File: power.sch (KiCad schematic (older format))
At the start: 68 parts, among them J1 PEN_SEL, J2 PEN_SEL, J3 USB_C_Receptacle_USB2.0, U10 74LVC1G02, U11 UTC2000, U4 TLV62569ADDC, U5 TPS62A01A-SOT563, U6 TPS62A01A-SOT563, U7 TLV62569ADDC, U9 TLV62569ADDC

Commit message: WIP: point before we change to OSH/relaxed process
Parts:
- added C91, C92: 100n, Capacitor_SMD:C_0603_1608Metric, symbol fmc:100nF_603
- added C93: 220u, Capacitor_Tantalum_SMD:CP_EIA-6032-28_Kemet-C, symbol Device:CP1_Small
- added C94: 1n, Capacitor_SMD:C_0603_1608Metric, symbol fmc:100nF_603
- added Q2: SSM6N35AFE, proj_footprints:SOT-563-adjusted, symbol Device:Q_DUAL_NMOS_S1G1D2S2G2D1
- added Q3: Si3477, Package_TO_SOT_SMD:TSOT-23-6, symbol fmc:Q_PMOS_DDGSDD
- added R75, R76, R78: 100k, Resistor_SMD:R_0603_1608Metric, symbol Device:R_Small
- added R77: 47, Resistor_SMD:R_1206_3216Metric, symbol Device:R_Small
- added R79: 10k, Resistor_SMD:R_0603_1608Metric, symbol Device:R_Small
- added U13: TPS3808DBV, Package_TO_SOT_SMD:SOT-23-6, symbol fmc:TPS3808DBV
- J1: value PEN_SEL -> CUR_SEL
- U10: value 74LVC1G02 -> 74VHC1G03; symbol fmc:74LVC1G02 -> fmc:74VHC1G03
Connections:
- net labels added: POWER_CYCLE
- wire segments 224 -> 267
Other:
- note added: "When using the inrush current limiter\nthe sense threshold matters!\nResistor values depend on TPS3808\nvariant's threshold!"
- note added: "optional inrush current\nlimiter (USB)."
- moved on the sheet: J1, J2, R52, R53, R62

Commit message: further work...
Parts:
- removed D9: LED, LED_SMD:LED_0603_1608Metric, symbol Device:LED
- removed R51: 1k, Resistor_SMD:R_0603_1608Metric, symbol Device:R_Small
- removed U10: 74VHC1G03, Package_TO_SOT_SMD:SOT-23-5, symbol fmc:74VHC1G03
- added Q6: Si3477, Package_TO_SOT_SMD:TSOT-23-6, symbol fmc:Q_PMOS_DDGSDD
- added Q7: SSM6N35AFE, proj_footprints:SOT-563-adjusted, symbol Device:Q_DUAL_NMOS_S1G1D2S2G2D1
- added TP14: TestPoint, TestPoint:TestPoint_Pad_D1.0mm, symbol Connector:TestPoint
- added U10: 74LVC1G06, Package_TO_SOT_SMD:SOT-353_SC-70-5, symbol fmc:74LVC1G38
- J2: footprint Connector_PinHeader_2.54mm:PinHeader_2x03_P2.54mm_Vertical -> Connector_PinHeader_2.54mm:PinHeader_2x02_P2.54mm_Vertical; symbol Connector_Generic:Conn_02x03_Odd_Even -> Connector_Generic:Conn_02x02_Odd_Even
- R22, R23, R24, R25, R33: value 10k -> 100k
- R40: value 45.9k -> 10k
- R45: value 10.2k -> 45k3
- R52: value 100k -> 10k; Manufacturer Yageo -> (none); Part RC0603FR-07100KL -> (none)
- R75: value 100k -> 45.3k
- R76: value 100k -> 10k
- R77: value 47 -> 50; footprint Resistor_SMD:R_1206_3216Metric -> Resistor_SMD:R_0603_1608Metric
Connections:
- net +5V: now also Q6.4 (S), U10.5 (VCC); no longer R35.2, R52.2
- net GND: now also R35.2, R52.2, Q7.1 (S), Q7.4 (S), U10.3 (GND); no longer J2.6 (Pin_6)
- net PWR_EN: now also U10.4
- net USB_BCDb: now also R35.1, Q7.2 (G); no longer J2.2 (Pin_2)
- net USB_PWRENb: now also R52.1, Q7.5 (G); no longer J2.4 (Pin_4)
- net at J1.1 (Pin_1), J1.3 (Pin_3), J1.5 (Pin_5)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: now also U10.1, U10.2
- net at U9.5 (PG): now also TP14.1; no longer R35.1
- net at Q2.6 (D), Q3.3 (G), R78.2: now also Q6.3 (G)
- net at Q2.3 (D), U13.3 (~MR): now also J2.2 (Pin_2), J2.4 (Pin_4)
- new net: J2.1 (Pin_1), Q7.3 (D)
- new net: J2.3 (Pin_3), Q7.6 (D)
- new net +5V_SWITCHED: Q6.1 (D), Q6.2 (D), Q6.5 (D), Q6.6 (D)
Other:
- note added: "FIXME:\n- lemo/sma gpio\n- lan9254 refclock footprint"
- note added: "When using the inrush current limiter\nthe sense threshold matters!\nResistor values depend on TPS3808\nvariant's threshold!\nValues shown for 0.9V Version"
- note removed: "When using the inrush current limiter\nthe sense threshold matters!\nResistor values depend on TPS3808\nvariant's threshold!"
- moved on the sheet: C54, C55, C62, C63, C64, C65, C66, C67, C68, C69, C70, C71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

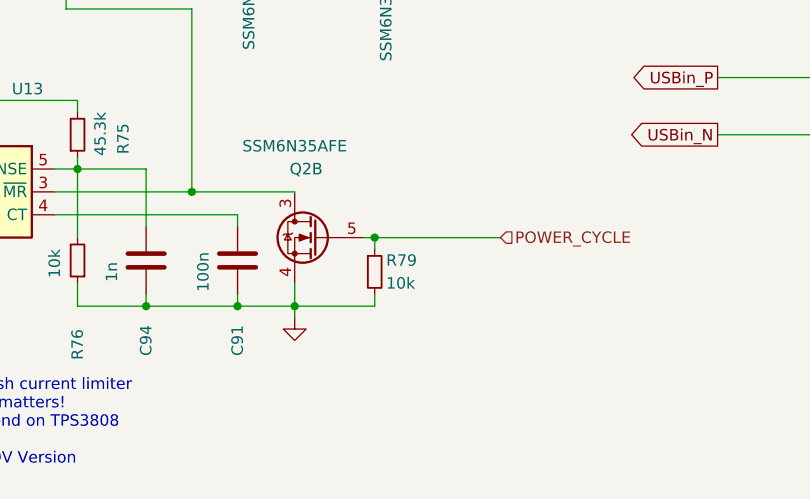
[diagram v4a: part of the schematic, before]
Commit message: power.sch: changed R79 from 10k to 1k
10k was not enough to overcome fpga-internal pullup (while device
unconfigured) and would result in power-cycle.
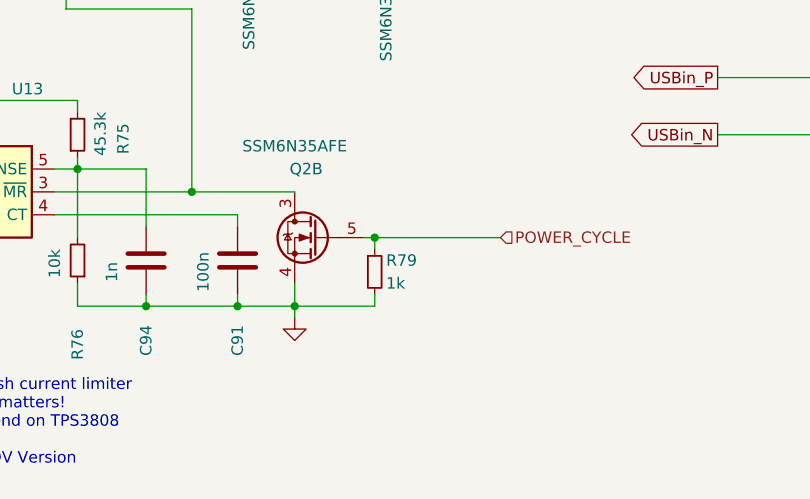
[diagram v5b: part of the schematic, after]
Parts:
- R79: value 10k -> 1k
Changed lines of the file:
@@
 AR Path="/61FBA485/623A16A6" Ref="R79"  Part="1"
 F 0 "R79" H 6950 6350 50  0000 L CNN
-F 1 "10k" H 6950 6250 50  0000 L CNN
+F 1 "1k" H 6950 6250 50  0000 L CNN
 F 2 "Resistor_SMD:R_0603_1608Metric" H 6900 6300 50  0001 C CNN
 F 3 "~" H 6900 6300 50  0001 C CNN
